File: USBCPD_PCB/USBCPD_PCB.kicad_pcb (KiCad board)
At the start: 2 copper layers, 64 parts, among them IC1 TMCS1108A3BQDRQ1, IC2 UCC27282QDRQ1, IC3 UCC27282QDRQ1, IC4 BAJ2CC0FP-E2, J1 TB002-500-02BE, J2 TB002-500-02BE, Q1 SIR584DP-T1-RE3, Q2 SIR584DP-T1-RE3, Q3 SIR584DP-T1-RE3, Q4 SIR584DP-T1-RE3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

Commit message: PCB layout, components sorted
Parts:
- moved C8 83.2 mm to (129.3, 71.1)
- moved C3 83.1 mm to (132.6, 109.2), turned to 180 degrees
- moved C5 77.7 mm to (132.6, 105.7), turned to 180 degrees
- moved IC1 77.5 mm to (131.1, 57.7), turned to 90 degrees
- moved LED3 77.4 mm to (160.5, 59.7)
- moved LED2 77.2 mm to (143.3, 64.3)
- moved JP1 73.6 mm to (159.7, 67.3)
- moved Q1 70.7 mm to (131.8, 100.3), turned to 180 degrees
- moved R10 69.0 mm to (143.3, 62.2)
- moved D2 66.6 mm to (124.7, 84.8)
- moved J1 66.3 mm to (131.6, 128.1)
- moved C6 66.0 mm to (131.1, 87.9), turned to 180 degrees
- moved C7 62.8 mm to (131.1, 84.6), turned to 180 degrees
- moved C13 61.9 mm to (143.5, 78.2)
- moved C16 61.8 mm to (139.2, 82.3), turned to -90 degrees
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
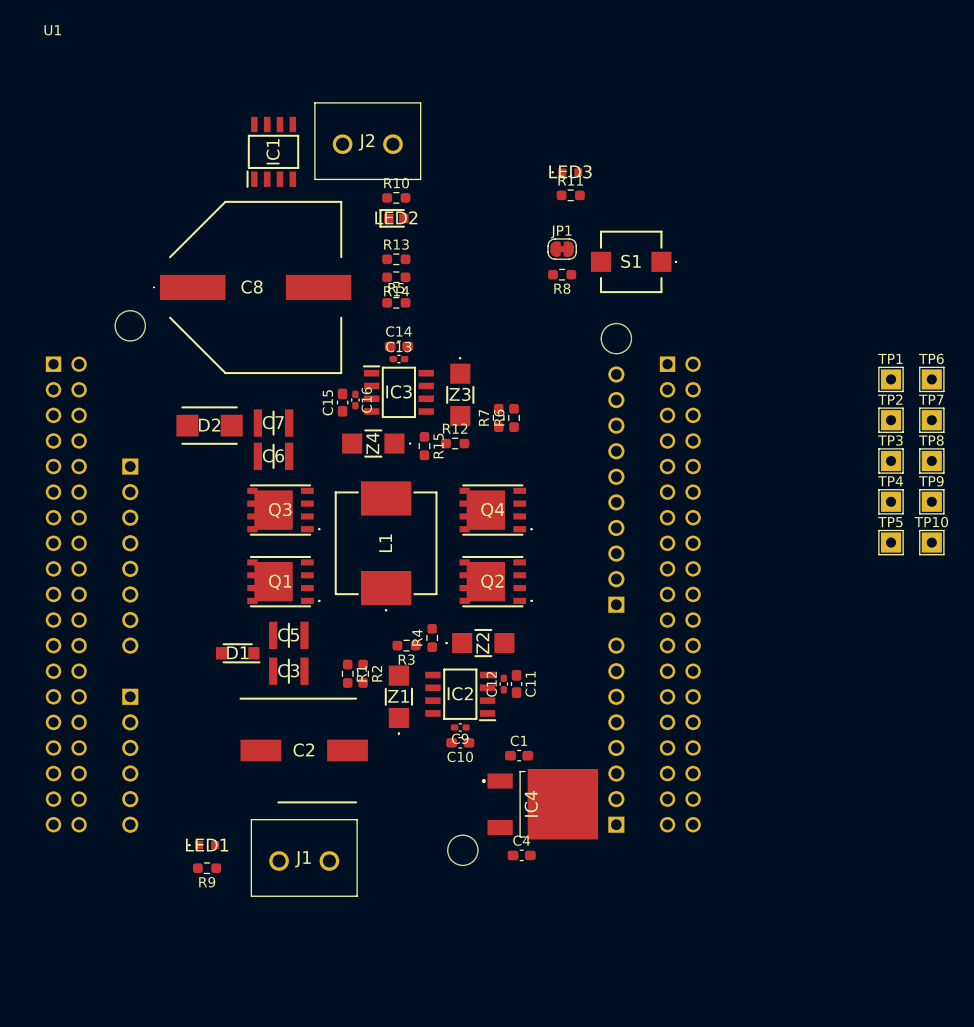
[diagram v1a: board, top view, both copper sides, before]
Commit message: Schematic Fixes, Routing started
Removed big zener diodes, replaced with smaller ones
started routing
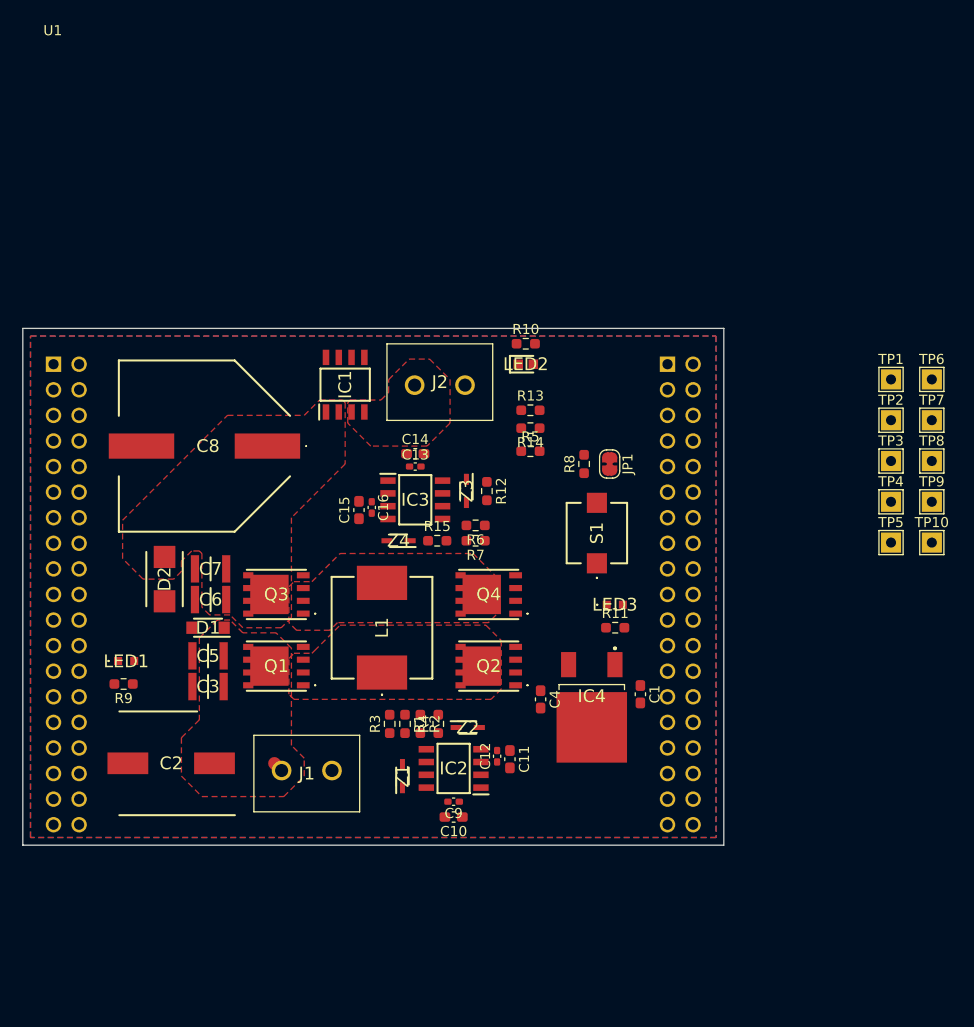
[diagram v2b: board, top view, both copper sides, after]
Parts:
- Z1, Z2, Z3, Z4: value PTZTFTE2515B -> PDZ15B,115; footprint SamacSys_Parts:PTZTFTE2515B -> SamacSys_Parts:SOD2512X110N
- moved LED3 43.2 mm to (164.9, 102.6)
- moved R11 43.2 mm to (165.0, 104.9)
- moved S1 27.1 mm to (163.2, 95.5), turned to 90 degrees
- moved J2 25.0 mm to (145.1, 80.8)
- moved IC1 24.2 mm to (138.2, 80.8)
- moved JP1 21.9 mm to (164.4, 88.6), turned to -90 degrees
- moved R9 20.1 mm to (116.2, 110.5)
- moved R13 20.0 mm to (156.6, 83.3)
- moved R14 20.0 mm to (156.6, 85.1)
- moved LED1 20.0 mm to (116.4, 108.2)
- moved R5 19.9 mm to (156.6, 87.4)
- moved R10 19.4 mm to (156.1, 76.7)
- moved LED2 19.4 mm to (156.1, 78.7)
- moved R8 18.9 mm to (161.9, 88.6), turned to 90 degrees
- moved C8 16.5 mm to (124.2, 86.9), turned to 180 degrees
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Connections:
- J1 pad 1: VBUS -> GND
- J1 pad 2: GND -> VBUS
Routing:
- net VBUS: track 0.00 -> 2.72 mm
- added copper zone on F.Cu, net +BATT
- added copper zone on B.Cu, net GND
- added copper zone on F.Cu, net GND
- added copper zone on F.Cu, net Net-(IC1-IN-_1)
- added copper zone on F.Cu, net Q1_S
- added copper zone on F.Cu, net Q3_S
- added copper zone on F.Cu, net VBUS
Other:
- board outline added: 69.6 x 51.3 mm

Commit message: more routing
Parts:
- removed TP1, TP10, TP2, TP3, TP4, TP5, TP6, TP7, TP8, TP9: TestPoint, TestPoint:TestPoint_THTPad_2.0x2.0mm_Drill1.0mm
- moved R9 4.85 mm to (114.3, 106.0), turned to -90 degrees
- moved LED2 4.84 mm to (160.8, 80.0)
- moved R10 4.84 mm to (160.8, 78.0)
- moved R13 4.21 mm to (160.8, 83.3)
- moved R14 4.21 mm to (160.8, 85.1)
- moved R5 4.21 mm to (160.8, 87.4)
- moved R3 3.20 mm to (145.8, 114.5)
- moved LED1 2.56 mm to (114.6, 109.9), turned to -90 degrees
- moved R1 2.51 mm to (143.4, 116.8), turned to 0 degrees
- moved R2 2.44 mm to (143.4, 115.3), turned to 0 degrees
- moved C10 2.20 mm to (151.1, 123.4)
- moved C9 2.19 mm to (151.1, 122.2)
- moved C13 2.07 mm to (143.1, 88.9)
- moved R8 1.96 mm to (163.8, 89.0)
- moved JP1 1.95 mm to (166.4, 88.9)
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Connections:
- R7 pad 1: PB13_PWM -> PB14_PWM
- U1 pad CN10_30: PB13_PWM -> PB14_PWM
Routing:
- net GND: track 0.00 -> 145.3 mm, vias 0 -> 82
- net PB14_PWM: track 0.00 -> 88.7 mm, vias 0 -> 2
- net +12V: track 0.00 -> 58.7 mm, vias 0 -> 2
- net PA8_PWM: track 0.00 -> 51.9 mm
- net PA9_PWM: track 0.00 -> 51.1 mm
- net PA10_ADC_Vout: track 0.00 -> 49.5 mm
- net +3.3V: track 0.00 -> 44.2 mm
- net PB3_ADC_Iout: track 0.00 -> 40.5 mm, vias 0 -> 1
- net +BATT: track 0.00 -> 37.1 mm, vias 0 -> 2
- net VBUS: track 2.72 -> 34.6 mm, vias 0 -> 2
- net Net-(IC1-VOUT): track 0.00 -> 31.2 mm
- net Q1_PWM: track 0.00 -> 21.3 mm
- net PB12_LED: track 0.00 -> 18.5 mm
- net Q3_S: track 0.00 -> 17.0 mm
- net Q3_PWM: track 0.00 -> 15.6 mm
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
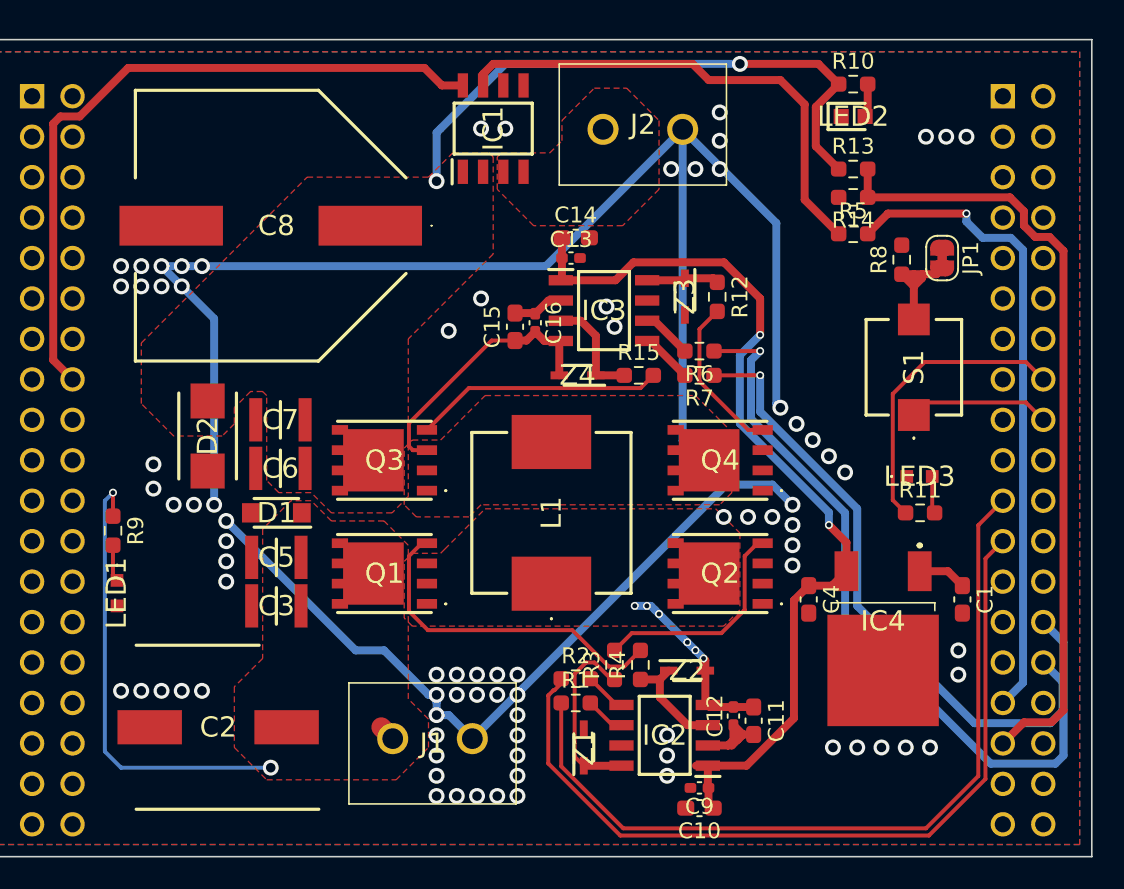
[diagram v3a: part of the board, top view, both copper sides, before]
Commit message: libs added, routing finalized, fixed issues
copied libs into folder, wrong wiring fixed, added test pads and silkscreen
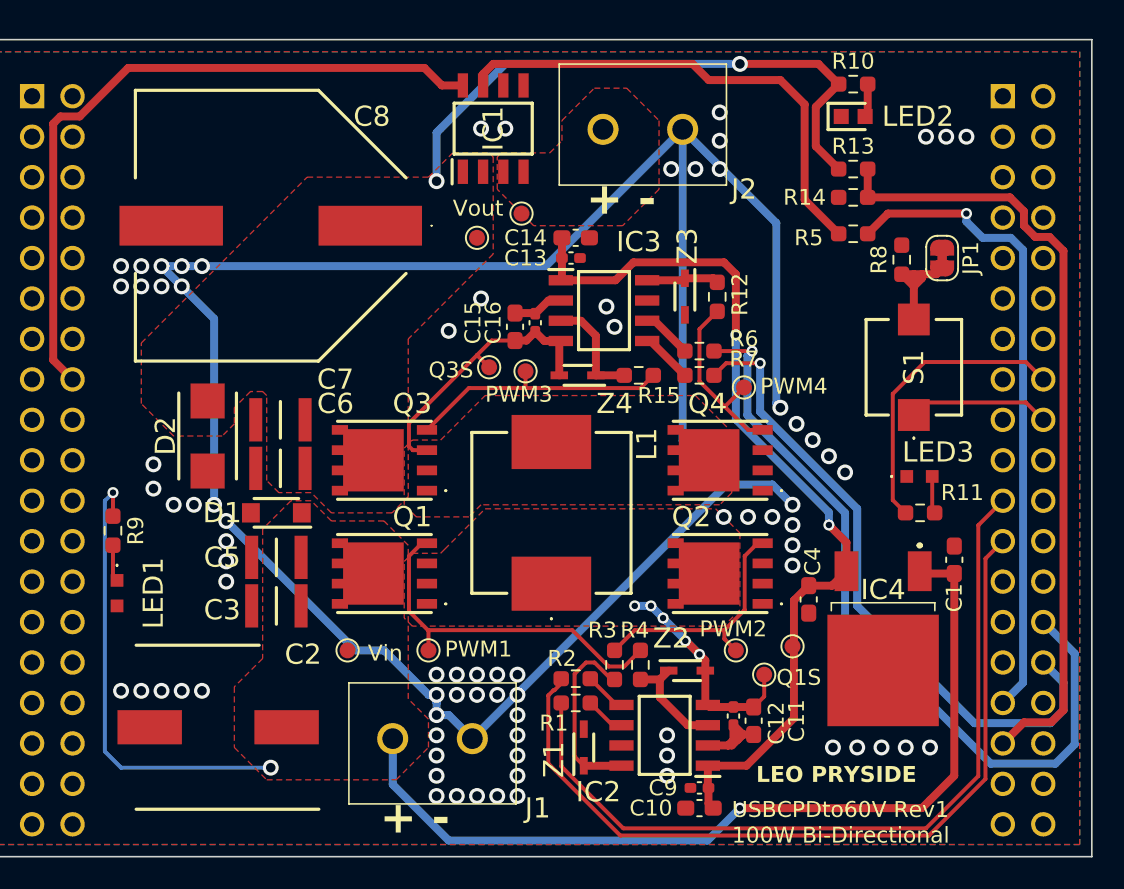
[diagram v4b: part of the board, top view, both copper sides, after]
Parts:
- added TP1: TestPoint, TestPoint:TestPoint_Pad_D1.0mm, F.Cu at (157.0, 113.3)
- added TP10: TestPoint, TestPoint:TestPoint_Pad_D1.0mm, F.Cu at (153.9, 97.0)
- added TP2: TestPoint, TestPoint:TestPoint_Pad_D1.0mm, F.Cu at (129.0, 113.5)
- added TP3: TestPoint, TestPoint:TestPoint_Pad_D1.0mm, F.Cu at (155.2, 115.1)
- added TP4: TestPoint, TestPoint:TestPoint_Pad_D1.0mm, F.Cu at (137.9, 95.8)
- added TP5: TestPoint, TestPoint:TestPoint_Pad_D1.0mm, F.Cu at (137.2, 87.6)
- added TP6: TestPoint, TestPoint:TestPoint_Pad_D1.0mm, F.Cu at (134.1, 113.5)
- added TP7: TestPoint, TestPoint:TestPoint_Pad_D1.0mm, F.Cu at (153.4, 113.5)
- added TP8: TestPoint, TestPoint:TestPoint_Pad_D1.0mm, F.Cu at (140.0, 86.1)
- added TP9: TestPoint, TestPoint:TestPoint_Pad_D1.0mm, F.Cu at (140.2, 96.0)
- moved C1 2.54 mm to (167.1, 107.8), turned to 90 degrees
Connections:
- R7 pad 1: PB14_PWM -> PB13_PWM
- U1 pad CN10_20: unconnected-(U1B-GND-PadCN10_20) -> GND
- U1 pad CN10_30: PB14_PWM -> PB13_PWM
- U1 pad CN10_9: unconnected-(U1B-GND-PadCN10_9) -> GND
- U1 pad CN7_19: unconnected-(U1A-GND-PadCN7_19) -> GND
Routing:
- net VBUS: track 34.6 -> 86.7 mm, vias 2 -> 3
- net PB13_PWM: track 0.00 -> 40.8 mm, vias 0 -> 1
- net PB14_PWM: track 88.7 -> 49.0 mm, vias 2 -> 1
- net Q1_S: track 11.6 -> 15.2 mm, vias 6 -> 5
- net +12V: track 58.7 -> 56.9 mm
- net Q4_PWM: track 10.1 -> 11.8 mm
- net Q2_PWM: track 14.1 -> 15.6 mm
- net Q1_PWM: track 21.3 -> 22.6 mm
- net Q3_S: track 17.0 -> 18.1 mm
- net Q3_PWM: track 15.6 -> 16.7 mm
- net GND: vias 82 -> 80
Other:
- board text added: "+ -"
- board text added: "LEO PRYSIDE"
- board text added: "PWM1"
- board text added: "PWM2"
- board text added: "PWM3"
- board text added: "PWM4"
- board text added: "Q1S"
- board text added: "Q3S"
- board text added: "USBCPDto60V Rev1 100W Bi-Directional"
- board text added: "Vin"
- board text added: "Vout"

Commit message: pcb design fixes
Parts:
- moved LED2 4.15 mm to (164.9, 79.2)
- moved R10 4.15 mm to (164.9, 77.2)
- moved R13 4.15 mm to (164.9, 82.5)
- moved R14 4.15 mm to (164.9, 84.3)
- moved R5 4.15 mm to (164.9, 86.6)
- moved TP5 1.55 mm to (137.4, 86.1)
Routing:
- net PB3_ADC_Iout: track 40.5 -> 35.4 mm
- net PA10_ADC_Vout: track 49.5 -> 45.7 mm
- net Net-(IC1-VOUT): track 31.2 -> 35.0 mm
- net +BATT: track 37.1 -> 40.0 mm

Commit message: drc fixes
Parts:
- moved R5 0.25 mm to (164.9, 86.4)
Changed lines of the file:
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@@
     (property "ki_keywords" "R res resistor")
     (attr smd)
-    (fp_text reference "R13" (at 0 -1.43) (layer "F.SilkS")
+    (fp_text reference "R13" (at 3.036 0) (layer "F.SilkS")
         (effects (font (size 1 1) (thickness 0.15)))
     )
@@
     (property "ki_keywords" "R res resistor")
     (attr smd)
-    (fp_text reference "R10" (at 0 -1.43) (layer "F.SilkS")
+    (fp_text reference "R10" (at 3.036 0) (layer "F.SilkS")
         (effects (font (size 1 1) (thickness 0.15)))
     )
@@
   )
   (footprint "Resistor_SMD:R_0603_1608Metric_Pad0.98x0.95mm_HandSolder" (layer "F.Cu")
-    (at 164.858 86.614)
+    (at 164.858 86.36)
     (descr "Resistor SMD 0603 (1608 Metric), square (rectangular) end terminal, IPC_7351 nominal with elongated pad for handsoldering. (Body size source: IPC-SM-782 page 72, https://www.pcb-3d.com/wordpress/wp-content/uploads/ipc-sm-782a_amendment_1_and_2.pdf), generated with kicad-footprint-generator")
     (tags "resistor handsolder")
@@
     (property "ki_keywords" "R res resistor")
     (attr smd)
-    (fp_text reference "R5" (at -2.794 0.254) (layer "F.SilkS")
+    (fp_text reference "R5" (at 2.528 0) (layer "F.SilkS")
         (effects (font (size 1 1) (thickness 0.15)))
     )
@@
     (property "ki_keywords" "R res resistor")
     (attr smd)
-    (fp_text reference "R14" (at 3.048 0) (layer "F.SilkS")
+    (fp_text reference "R14" (at -3.036 0) (layer "F.SilkS")
         (effects (font (size 1 1) (thickness 0.15)))
     )
@@
   (segment (start 140.775 92.3555) (end 140.816 92.3965) (width 0.5) (layer "F.Cu") (net 8))
   (segment (start 139.546 92.3555) (end 140.775 92.3555) (width 0.5) (layer "F.Cu") (net 8))
-  (segment (start 162.052 84.7205) (end 163.9455 86.614) (width 0.5) (layer "F.Cu") (net 11))
-  (segment (start 161.036 77.724) (end 162.052 78.74) (width 0.5) (layer "F.Cu") (net 11))
-  (segment (start 137.541 78.061) (end 137.541 77.342) (width 0.5) (layer "F.Cu") (net 11))
-  (segment (start 151.711503 77.724) (end 161.036 77.724) (width 0.5) (layer "F.Cu") (net 11))
-  (segment (start 137.541 77.342) (end 138.175 76.708) (width 0.5) (layer "F.Cu") (net 11))
-  (segment (start 162.052 78.74) (end 162.052 84.7205) (width 0.5) (layer "F.Cu") (net 11))
-  (segment (start 150.695503 76.708) (end 151.711503 77.724) (width 0.5) (layer "F.Cu") (net 11))
-  (segment (start 138.175 76.708) (end 150.695503 76.708) (width 0.5) (layer "F.Cu") (net 11))
+  (segment (start 163.9455 86.36) (end 162.052 84.4665) (width 0.5) (layer "F.Cu") (net 11))
+  (segment (start 137.541 77.342) (end 137.541 78.061) (width 0.5) (layer "F.Cu") (net 11))
+  (segment (start 151.711503 77.724) (end 150.695503 76.708) (width 0.5) (layer "F.Cu") (net 11))
+  (segment (start 162.052 78.74) (end 161.036 77.724) (width 0.5) (layer "F.Cu") (net 11))
+  (segment (start 162.052 84.4665) (end 162.052 78.74) (width 0.5) (layer "F.Cu") (net 11))
+  (segment (start 161.036 77.724) (end 151.711503 77.724) (width 0.5) (layer "F.Cu") (net 11))
+  (segment (start 150.695503 76.708) (end 138.175 76.708) (width 0.5) (layer "F.Cu") (net 11))
+  (segment (start 138.175 76.708) (end 137.541 77.342) (width 0.5) (layer "F.Cu") (net 11))
   (segment (start 133.858 76.962) (end 134.957 78.061) (width 0.5) (layer "F.Cu") (net 12))
   (segment (start 112.20827 80.01) (end 115.25627 76.962) (width 0.5) (layer "F.Cu") (net 12))
@@
   (segment (start 146.157604 125.164) (end 165.540396 125.164) (width 0.25) (layer "F.Cu") (net 30))
   (segment (start 141.6345 120.640896) (end 146.157604 125.164) (width 0.25) (layer "F.Cu") (net 30))
-  (segment (start 165.7705 86.614) (end 167.894 86.614) (width 0.5) (layer "F.Cu") (net 31))
+  (segment (start 165.7705 86.36) (end 167.64 86.36) (width 0.5) (layer "F.Cu") (net 31))
+  (segment (start 167.64 86.36) (end 167.894 86.614) (width 0.5) (layer "F.Cu") (net 31))
   (via (at 167.894 86.614) (size 0.7) (drill 0.4) (layers "F.Cu" "B.Cu") (net 31))
   (segment (start 171.45 115.57) (end 170.18 116.84) (width 0.5) (layer "B.Cu") (net 31))

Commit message: gerber files created + small fixes
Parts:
- added G***: LOGO, Logos:hhn_logo, F.Cu at (157.2, 86.1)
